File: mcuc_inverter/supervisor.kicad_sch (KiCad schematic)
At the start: 0 parts

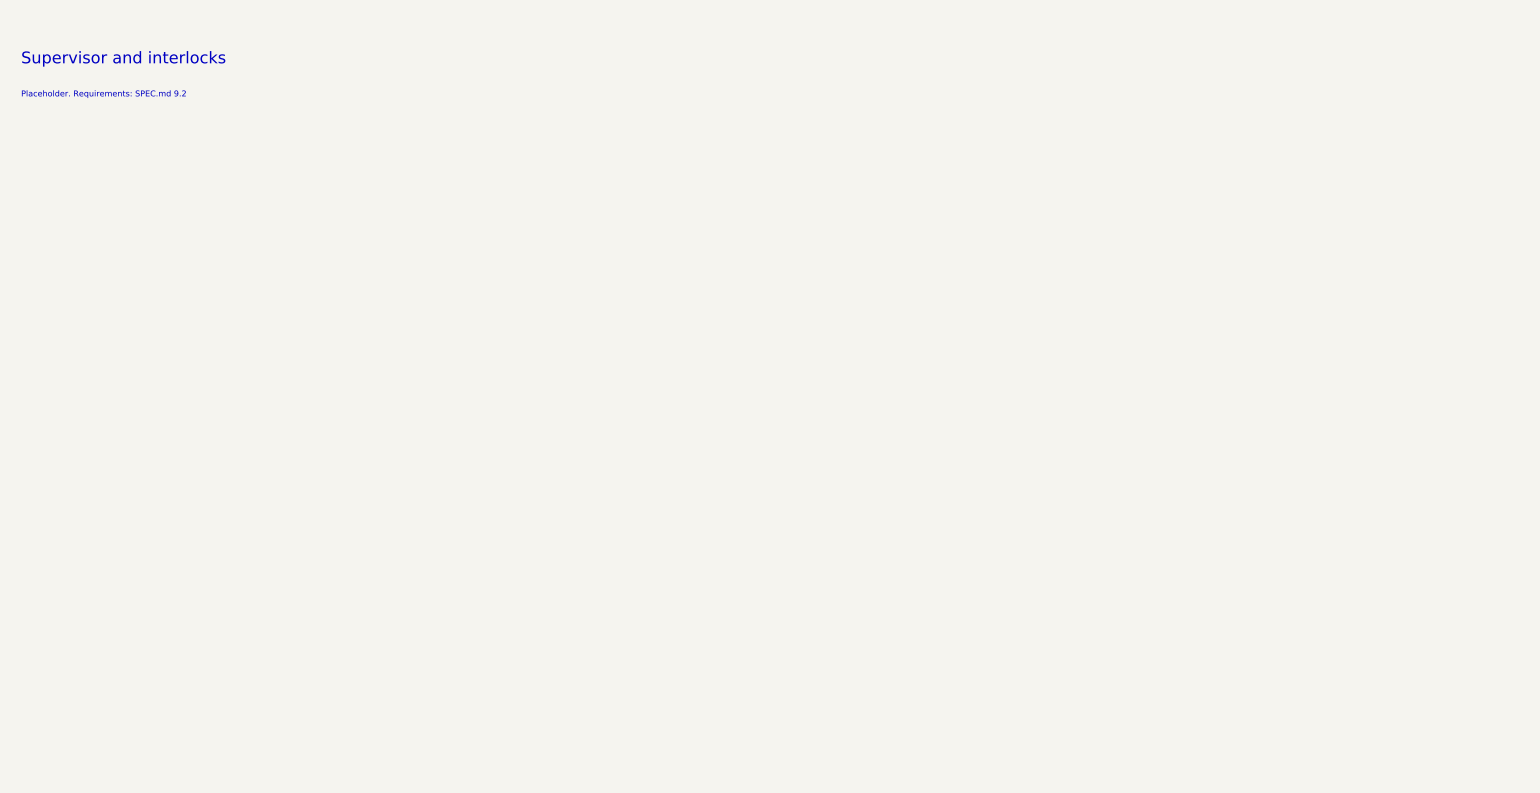
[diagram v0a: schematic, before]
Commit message: Port PALTA supervisor interlocks to KiCad 9 supervisor sheet
Faithful recapture of pcb_design/supervisor.sch (verified against the
legacy VESC-controller.net netlist): per-phase NAND overlap detection
gating complementary PWM pairs through AND gates (both outputs forced
low on overlap), 4.7k boot pulldowns on all six PWM inputs, AUP1G74
overcurrent latch (OC_TRIP edge -> latched, FAULT_RESET clear, LED),
driver-fault conditioning (RC + BAT54S clamp) driving FAULT_BKIN, and
the active-low driver-reset chain (MCU request AND driver-fault AND
OC latch).

Interface: PWM_HS/LS_1..3 in, *_GATED out, OC_TRIP (single open-drain
input; comparator lives with current sensing per SPEC), DRV_FAULT_IN,
OC_LATCHED, FAULT_RESET, DRV_RST_IN/OUT. Root sheet wires the six PWM
nets and FAULT_BKIN between MCU and supervisor; FAULT_BKIN verified by
netlist to land on U1 pin 51 = PB12 (TIM1_BKIN).

ERC 0 errors. 24/24 gate-by-gate netlist checks against the legacy
reconstruction pass. Deviations recorded on-sheet: all-3.3V logic
(original BOM fitted ACT08 at 5 V), added pullups on FAULT_RESET /
DRV_RST_IN boot state.

Finding: the original circuit performs overlap elimination only - it
contains NO hardware dead-time insertion despite D008/SPEC 9.2 claiming
it. Recorded separately as a spec discrepancy.

Co-Authored-By: Claude Fable 5 <noreply@anthropic.com>
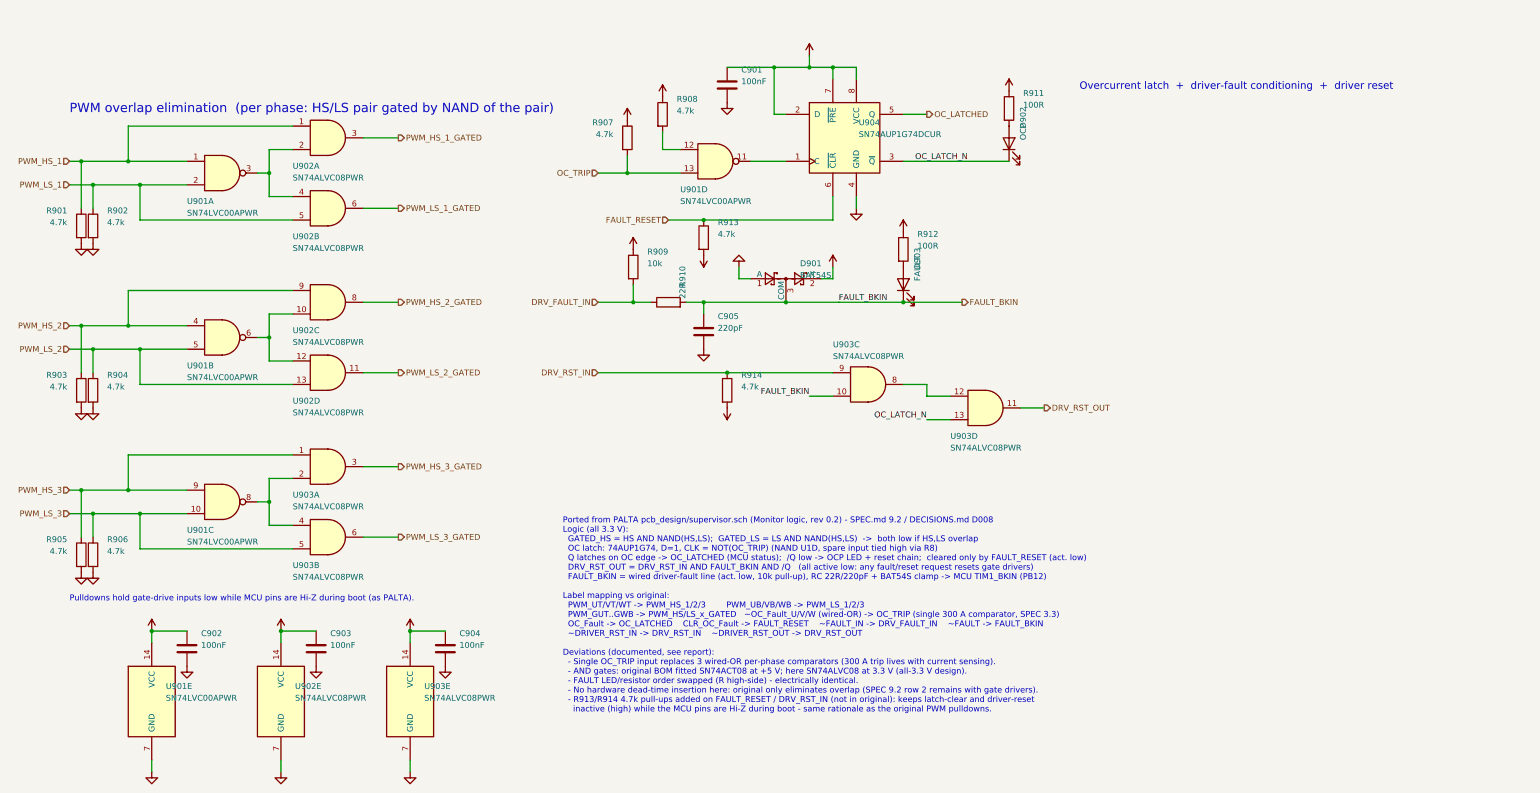
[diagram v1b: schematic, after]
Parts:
- added C901, C902, C903, C904: 100nF, Capacitor_SMD:C_0603_1608Metric, symbol Device:C
- added C905: 220pF, Capacitor_SMD:C_0603_1608Metric, symbol Device:C
- added D901: BAT54S, Package_TO_SOT_SMD:SOT-23, symbol Diode:BAT54S
- added D902: OCP, LED_SMD:LED_0603_1608Metric, symbol Device:LED
- added D903: FAULT, LED_SMD:LED_0603_1608Metric, symbol Device:LED
- added R901, R902, R903, R904, R905, R906, R907, R908, R913, R914: 4.7k, Resistor_SMD:R_0603_1608Metric, symbol Device:R
- added R909: 10k, Resistor_SMD:R_0603_1608Metric, symbol Device:R
- added R910: 22R, Resistor_SMD:R_0603_1608Metric, symbol Device:R
- added R911, R912: 100R, Resistor_SMD:R_0603_1608Metric, symbol Device:R
- added U901: SN74LVC00APWR, Package_SO:TSSOP-14_4.4x5mm_P0.65mm, symbol 74xx:74LS00
- added U902, U903: SN74ALVC08PWR, Package_SO:TSSOP-14_4.4x5mm_P0.65mm, symbol 74xx:74LS08
- added U904: SN74AUP1G74DCUR, Package_SO:VSSOP-8_2.3x2mm_P0.5mm, symbol 74xGxx:74AUP1G74
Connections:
- new net: U901.8, U903.2, U903.4
- new net: U901.11, U904.1 (C)
- new net: R908.2, U901.12
- new net: U901.3, U902.2, U902.4
- new net: U903.12, U903.8
- new net: D902.2 (A), R911.2
- new net: U901.6, U902.10, U902.12
- new net: D903.2 (A), R912.2
- new net +3.3V: C901.1, C902.1, C903.1, C904.1, D901.2 (K), R907.1, R908.1, R909.1, R911.1, R912.1, R913.2, R914.2, U901.14 (VCC), U902.14 (VCC), U903.14 (VCC), U904.2 (D), U904.7 (~{PRE}), U904.8 (VCC)
- new net DRV_FAULT_IN: R909.2, R910.1
- new net DRV_RST_IN: R914.1, U903.9
- new net DRV_RST_OUT: U903.11
- new net FAULT_BKIN: C905.1, D901.3 (COM), D903.1 (K), R910.2, U903.10
- new net FAULT_RESET: R913.1, U904.6 (~{CLR})
- new net GND: C901.2, C902.2, C903.2, C904.2, C905.2, D901.1 (A), R901.2, R902.2, R903.2, R904.2, R905.2, R906.2, U901.7 (GND), U902.7 (GND), U903.7 (GND), U904.4 (GND)
- new net OC_LATCHED: U904.5 (Q)
- new net OC_LATCH_N: D902.1 (K), U903.13, U904.3 (~{Q})
- new net OC_TRIP: R907.2, U901.13
- new net PWM_HS_1: R901.1, U901.1, U902.1
- new net PWM_HS_1_GATED: U902.3
- new net PWM_HS_2: R903.1, U901.4, U902.9
- new net PWM_HS_2_GATED: U902.8
- new net PWM_HS_3: R905.1, U901.9, U903.1
- new net PWM_HS_3_GATED: U903.3
- new net PWM_LS_1: R902.1, U901.2, U902.5
- new net PWM_LS_1_GATED: U902.6
- new net PWM_LS_2: R904.1, U901.5, U902.13
- new net PWM_LS_2_GATED: U902.11
- new net PWM_LS_3: R906.1, U901.10, U903.5
- new net PWM_LS_3_GATED: U903.6
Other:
- note added: "Overcurrent latch + driver-fault conditioning + driver reset"
- note added: "PWM overlap elimination (per phase: HS/LS pair gated by NAND of the pair)"
- note added: "Ported from PALTA pcb_design/supervisor.sch (Monitor logic, rev 0.2) - SPEC.md 9.2 / DECISIONS.md D008 Logic (all 3.3 V): GATED_HS = HS AND NAND(HS,LS); GATED_LS = LS AND NAND(HS,LS) -> both low if HS,LS overlap OC latch: 74AUP1G74, D=1, CLK = NOT(OC_TRIP) (NAND U1D, spare input tied high via R8) Q latches on OC edge -> OC_LATCHED (MCU status); /Q low -> OCP LED + reset chain; cleared only by FAU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"
- note added: "Pulldowns hold gate-drive inputs low while MCU pins are Hi-Z during boot (as PALTA)."
- note removed: "Placeholder. Requirements: SPEC.md 9.2"
- note removed: "Supervisor and interlocks"

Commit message: Board-prep: footprint audit complete, HV terminals, off-board flags
474-component audit: 466 valid resolved footprints, 13 off-board
exclusions per D024 (caps to carrier, chassis resistors, HOYS), 4
flagged TBDs (custom flyback + 3 unchosen inductors), zero silent
gaps. Netlist-fatal fixes: Q403 renumbered to Wolfspeed TO-263-7
convention (G1/KS2/S3-7/tab-D8), CSD18543Q3A remapped to KiCad's
SSSGD VSON-8 pairing - both verified in the netlist afterward.

New HV interface terminals J401-J405 (M4 ring-lug pads: DC input,
precharge-R chassis loop, discharge-R return, bus taps) and HOYS
harness headers J501-J503 (JST 2mm; PA-vs-PH footprint flagged TBV)
with net membership machine-verified incl. the OC_TRIP wire-OR and
I_REF paths to the MCU ADCs.

ERC 0 errors, warnings 201 -> 200 (none introduced).

Co-Authored-By: Claude Fable 5 <noreply@anthropic.com>
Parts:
- D902, D903: footprint LED_SMD:LED_0603_1608Metric -> LED_SMD:LED_0805_2012Metric
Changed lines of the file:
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@@
 			)
 		)
-		(property "Footprint" "LED_SMD:LED_0603_1608Metric"
+		(property "Footprint" "LED_SMD:LED_0805_2012Metric"
 			(at 233.68 36.83 0)
 			(effects
@@
 			)
 		)
-		(property "Footprint" "LED_SMD:LED_0603_1608Metric"
+		(property "Footprint" "LED_SMD:LED_0805_2012Metric"
 			(at 210.82 67.31 0)
 			(effects

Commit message: Fix gate drive and supervisor: CR-1, CR-2, MJ-1, MJ-8, MJ-9, MJ-13
CR-1 - the fault-clear deadlock is broken. U903 gate 4 now computes
DRV_RST_OUT = DRV_RST_IN AND OC_LATCH_N; FAULT_BKIN is out of the
chain, so a rising RDYC edge is reachable. C907 (220 nF) gives a
1.03 ms power-on clear pulse, comfortably past the drivers' 200 us
start time and the 1.2 us minimum clear width, so the bridge comes
up without firmware intervention. Gate 3 is freed and labelled for
the discharge interlock.

MJ-1 - the overcurrent trip finally reaches TIM1_BKIN. D904 (BAT54WS)
wire-ORs OC_LATCH_N into FAULT_BKIN: 0.33 mA gives 0.31 V against a
0.95 V input-low threshold, and it reverse-biases on driver-only
faults so the two paths stay independent. SPEC 9.2's central claim is
now true as built.

CR-2 - DESAT reconfigured: ADJB linked to VCC1 (LEB 444 ns, filter
263 ns, was 650+1575), ADJA to 28.0k for the family-maximum 699 mA
soft-off, and the external blanking cap DNP'd because the datasheet
specifies all DESAT timing at 2 pF. Chain is now 1.9 us typical
against ~5.8 us before. Worst-case silicon reaches 2.6 us - see the
D026 amendment in the next commit; this is recorded, not rounded.

MJ-8 - added the VCC2-to-VEE2 capacitors that were missing on all six
domains. That is the loop carrying the gate pulse, and the datasheet
explicitly requires it.

MJ-9 - the -5 V off-rail had no defined bias: gate charge nets to zero
at COM, so the zener sat in its knee. 2.49k preloads (6.02 mA) per
isolated domain now hold it defined at 4.87 V, inside the module's
-5 V static maximum.

MJ-13 - LED resistors 100R -> 2.2k and D903 moved ahead of R910. The
fault wire-OR was being back-fed ~11 mA, pushing FAULT_BKIN to 0.94 V
against a 0.99 V threshold; it now sits at ~0.1 V.

MJ-17 - Miller clamp BSS138 -> BSS316N. Note the constraint the agent
found: CLAMPDRV swings to VEE2+11.5 V, so the +-12 V Vgs parts
suggested elsewhere are unusable; this is a +-20 V part.

MN-2 - documentation corrected to the tr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
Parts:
- added C906: 100n, Capacitor_SMD:C_0603_1608Metric, symbol Device:C
- added C907: 220n, Capacitor_SMD:C_0603_1608Metric, symbol Device:C
- added D904: BAT54WS, Diode_SMD:D_SOD-323, symbol Device:D
- D902: value OCP -> APT2012SURCK red (OCP)
- D903: value FAULT -> APT2012SYCK amber (DRV FLT)
- R911, R912: value 100R -> 2.2k
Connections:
- net DRV_FAULT_IN: now also D903.1 (K)
- net DRV_RST_IN: now also U903.12, C907.1; no longer U903.9
- net FAULT_BKIN: now also D904.2 (A); no longer D903.1 (K), U903.10
- net FAULT_RESET: now also C906.1
- net GND: now also U903.10, U903.9, C906.2, C907.2
- net OC_LATCH_N: now also D904.1 (K)
- net at U903.8: no longer U903.12
- no-connect marks 0 -> 1
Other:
- note added: "MJ-1: the 300 A overcurrent latch had NO path to TIM1_BKIN - it only reached the reset chain, so SPEC 9.2 was false as built. D904 pulls FAULT_BKIN low when OC_LATCH_N trips: 0.33 mA through R909 gives Vf ~0.28 V, so BKIN sits at ~0.31 V vs VIL 0.99 V. Reverse-biased when only a driver fault is present, so the latch is never back-fed."
- note added: "Ported from PALTA pcb_design/supervisor.sch (Monitor logic, rev 0.2) - SPEC.md 9.2 / DECISIONS.md D008 Logic (all 3.3 V): GATED_HS = HS AND NAND(HS,LS); GATED_LS = LS AND NAND(HS,LS) -> both low if HS,LS overlap OC latch: 74AUP1G74, D=1, CLK = NOT(OC_TRIP) (NAND U1D, spare input tied high via R8) Q latches on OC edge -> OC_LATCHED (MCU status); /Q low -> OCP LED + reset chain + FAULT_BKIN; cleare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"
- note added: "U903 gate 3 is now SPARE (CR-1). Inputs tied low, output open. Available if a discharge / bus-live interlock needs a gate."
- note removed: "Ported from PALTA pcb_design/supervisor.sch (Monitor logic, rev 0.2) - SPEC.md 9.2 / DECISIONS.md D008 Logic (all 3.3 V): GATED_HS = HS AND NAND(HS,LS); GATED_LS = LS AND NAND(HS,LS) -> both low if HS,LS overlap OC latch: 74AUP1G74, D=1, CLK = NOT(OC_TRIP) (NAND U1D, spare input tied high via R8) Q latches on OC edge -> OC_LATCHED (MCU status); /Q low -> OCP LED + reset chain; cleared only by FAU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"
- moved on the sheet: D903, R912, U903C
